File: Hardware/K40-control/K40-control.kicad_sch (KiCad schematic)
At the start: 11 parts

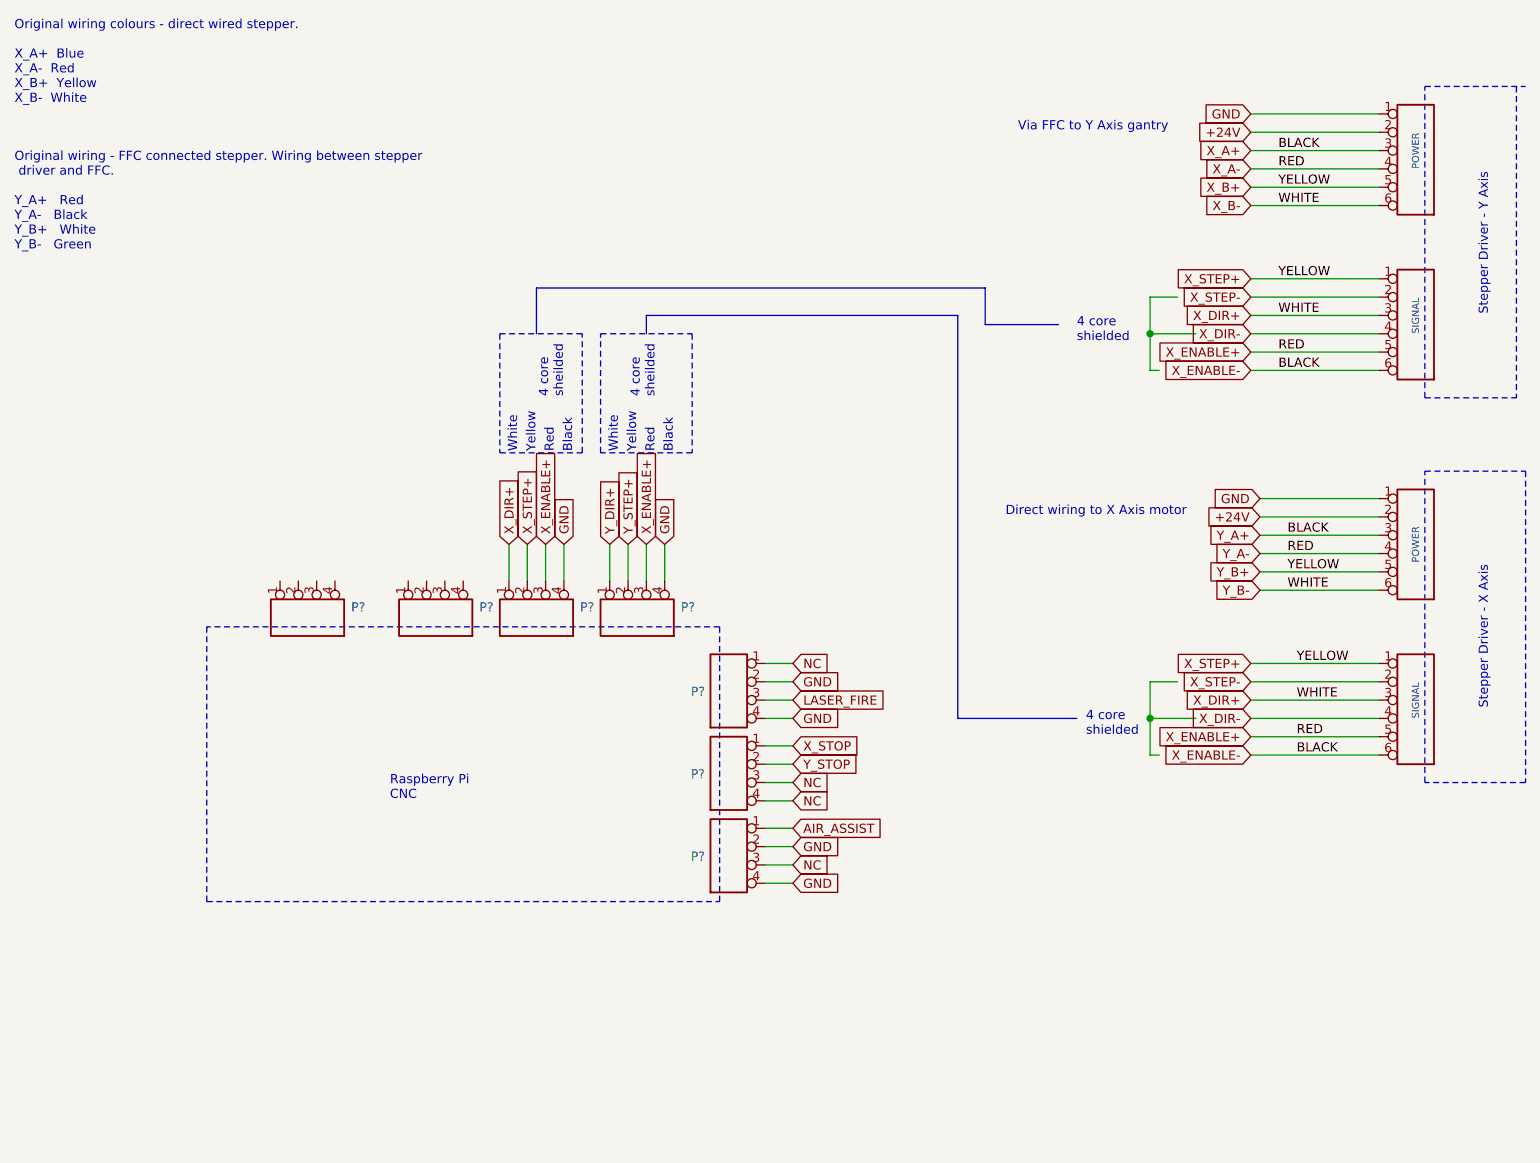
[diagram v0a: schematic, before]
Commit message: Added PDF of schematic
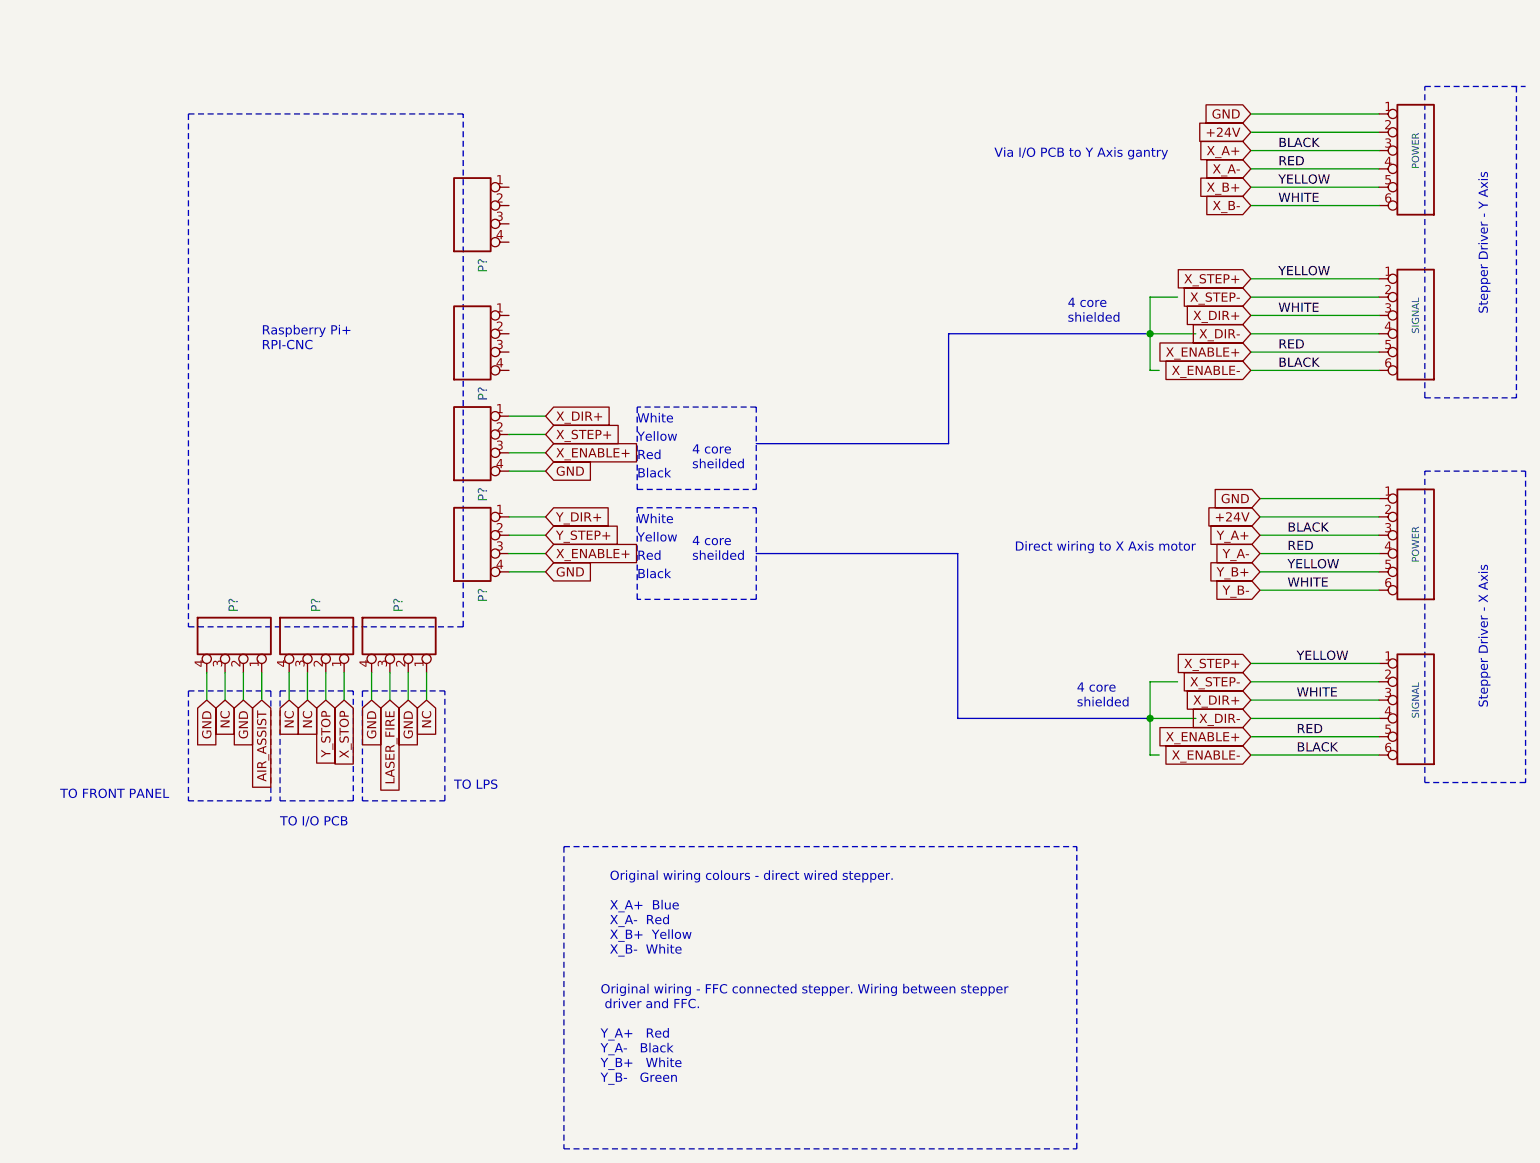
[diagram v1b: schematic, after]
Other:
- note added: "Raspberry Pi+ RPI-CNC"
- note added: "TO FRONT PANEL"
- note added: "TO I/O PCB"
- note added: "TO LPS"
- note added: "Via I/O PCB to Y Axis gantry"
- note removed: "Raspberry Pi CNC"
- note removed: "Via FFC to Y Axis gantry"
- company: Geoff Steer -> Hobart Makers
- moved on the sheet: P?
